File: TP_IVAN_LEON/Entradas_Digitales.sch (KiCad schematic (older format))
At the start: 7 parts, among them J1 Teclado

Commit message: Agregado codigo digey key en 80% de componentes
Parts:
- J1: Digikey# (none) -> WM1737-ND
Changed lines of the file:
@@
 F 2 "TP:Connector_Molex_PicoBlade_53047-0810" H 7750 3075 60  0001 C CNN
 F 3 "" H 7750 3075 60  0000 C CNN
+F 4 "WM1737-ND" H 7875 3075 60  0001 C CNN "Digikey#"
 	1    7875 3075
 	1    0    0    -1

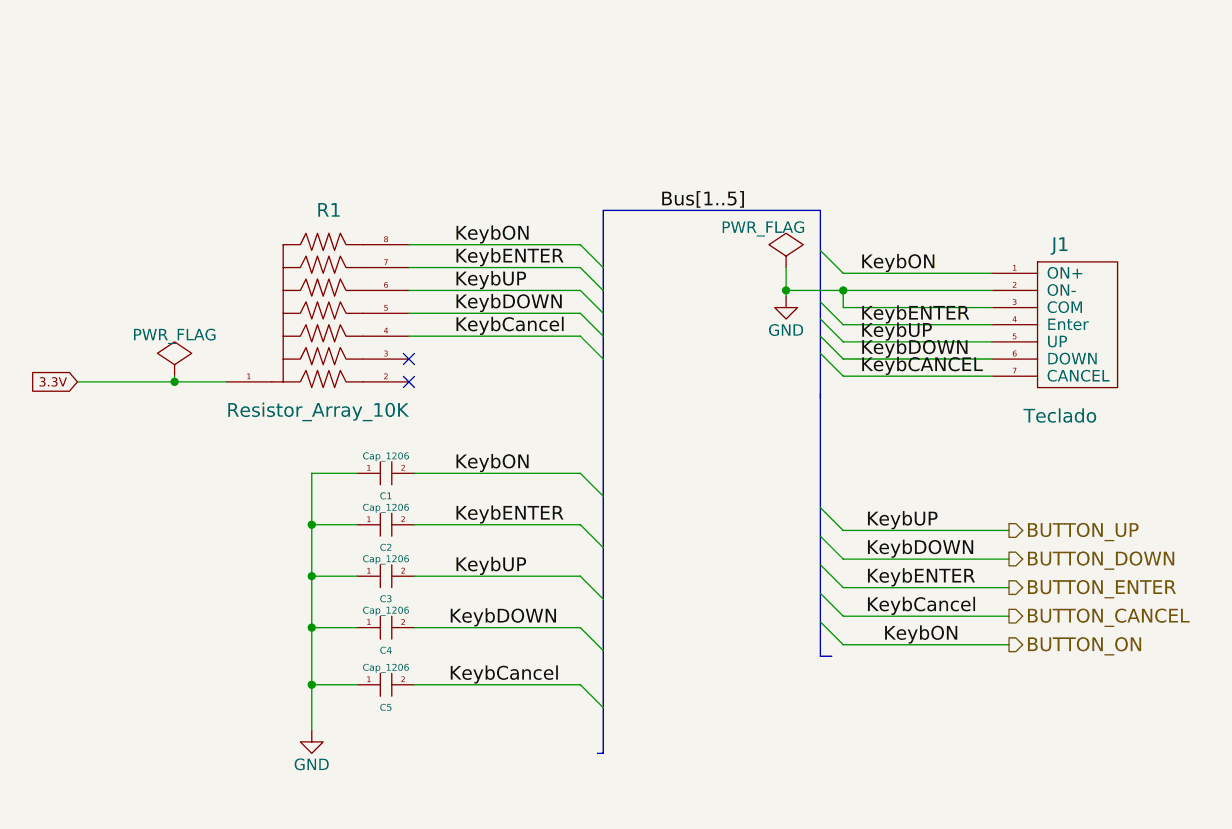
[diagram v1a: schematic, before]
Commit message: Agregado cambios subrayados en verde descritos en documento Leonv.ods en la carpeta docs
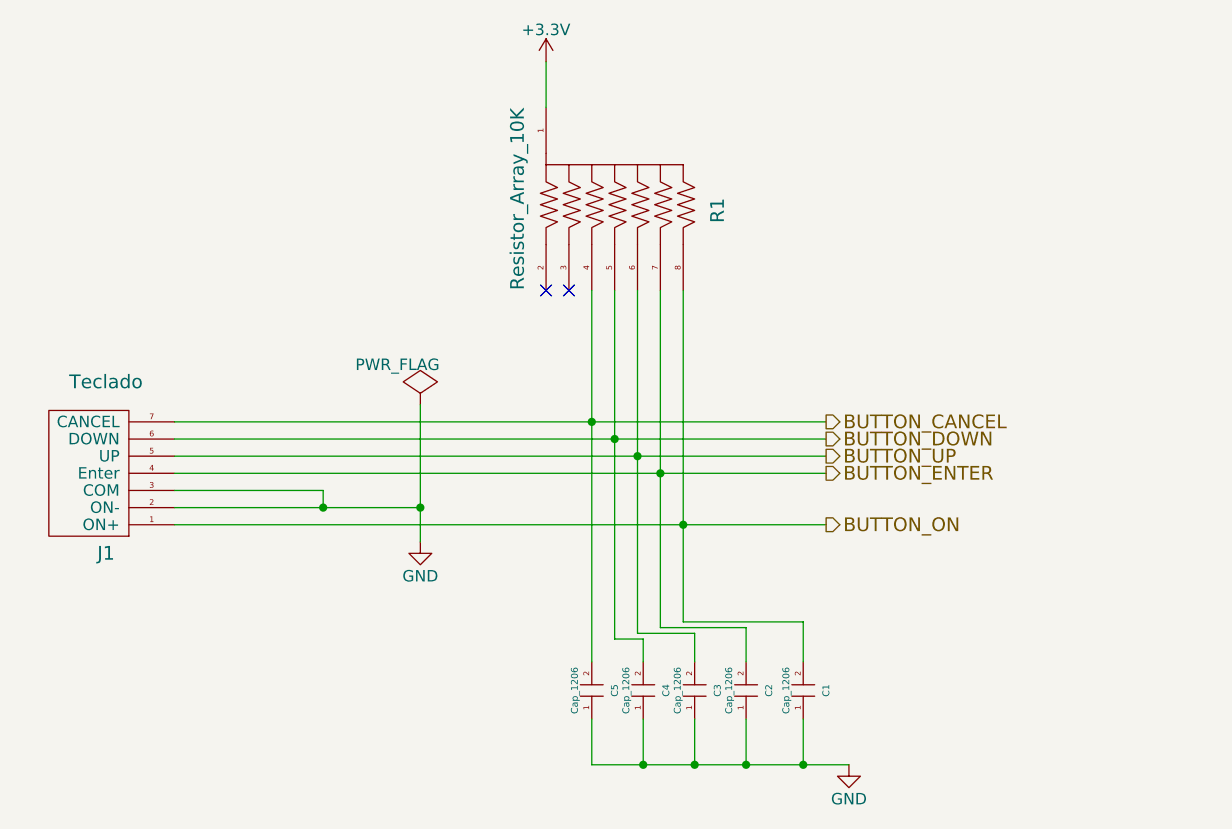
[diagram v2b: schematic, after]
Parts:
- renumbered C5 to C1, C4 to C2, C2 to C4, C1 to C5
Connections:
- net KeybCANCEL is gone; now on net BUTTON_CANCEL: J1.7 (CANCEL)
- net BUTTON_CANCEL: now also C5.2; no longer C1.2
- net BUTTON_DOWN: now also C4.2; no longer C2.2
- net BUTTON_ENTER: now also C2.2; no longer C4.2
- net BUTTON_ON: now also C1.2; no longer C5.2
- net 3.3V renamed +3V3
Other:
- moved on the sheet: C1, C2, C3, C4, C5, J1, R1

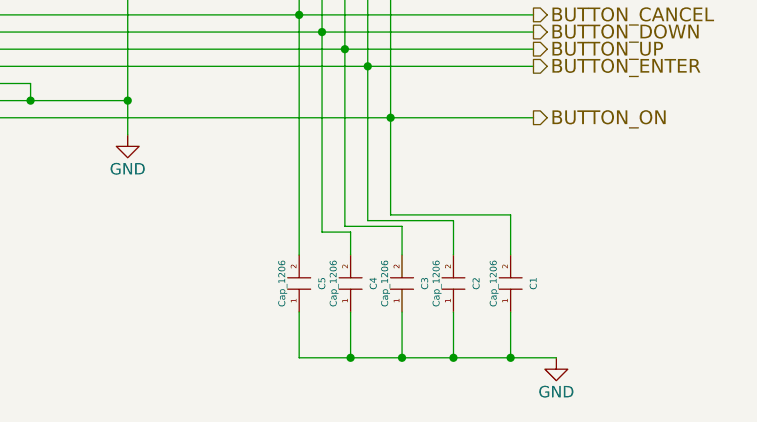
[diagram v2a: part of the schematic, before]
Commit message: Agrego Manf y Manf# en todos los componentes
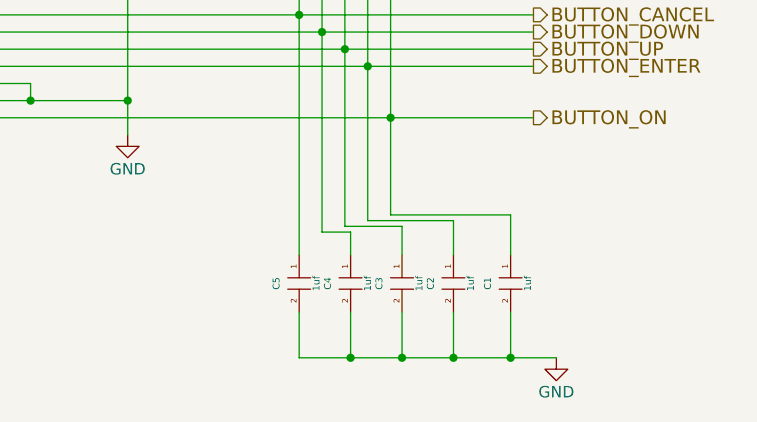
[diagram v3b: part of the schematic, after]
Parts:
- C1, C2, C3, C4, C5: value Cap_1206 -> 1uf; Digikey# (none) -> 399-1254-2-ND; Manf (none) -> Kemet; Manf# (none) -> C1206C105K4RACTU
- J1: Manf (none) -> Molex, LLC; Manf# (none) -> 0530470810
- R1: Digikey# (none) -> Y1747V0201BA0W-ND; Manf (none) -> Vishay Foil Resistors (Division of Vishay Precision Group); Manf# (none) -> Y1747V0201BA0W
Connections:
- net BUTTON_CANCEL: now also C5.1; no longer C5.2
- net BUTTON_DOWN: now also C4.1; no longer C4.2
- net BUTTON_ENTER: now also C2.1; no longer C2.2
- net BUTTON_ON: now also C1.1; no longer C1.2
- net BUTTON_UP: now also C3.1; no longer C3.2
- net GND: now also C1.2, C2.2, C3.2, C4.2, C5.2; no longer C1.1, C2.1, C3.1, C4.1, C5.1
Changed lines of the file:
@@
 F 3 "" H 3425 3675 60  0000 C CNN
 F 4 "WM1737-ND" H 3550 3675 60  0001 C CNN "Digikey#"
+F 5 "0530470810" H 3550 3675 60  0001 C CNN "Manf#"
+F 6 "Molex, LLC" H 3550 3675 60  0001 C CNN "Manf"
 	1    3550 3675
 	-1   0    0    1
@@
 F 2 "TP:Resistor_Array_SIP8" H 5900 2600 60  0001 C CNN
 F 3 "" H 5900 2600 60  0000 C CNN
+F 4 "Y1747V0201BA0W-ND" H 5975 2600 60  0001 C CNN "Digikey#"
+F 5 "Y1747V0201BA0W" H 5975 2600 60  0001 C CNN "Manf#"
+F 6 "Vishay Foil Resistors (Division of Vishay Precision Group)" H 5975 2600 60  0001 C CNN "Manf"
 	1    5975 2600
 	0    1    1    0
-$EndComp
-$Comp
-L Cap_1206 C5
-U 1 1 57846246
-P 5750 4650
-F 0 "C5" H 5750 4550 30  0000 C CNN
-F 1 "Cap_1206" H 5750 4725 30  0000 C CNN
-F 2 "TP:c_1206" H 5775 4650 60  0001 C CNN
-F 3 "" H 5775 4650 60  0000 C CNN
-	1    5750 4650
-	0    -1   -1   0
-$EndComp
-$Comp
-L Cap_1206 C4
-U 1 1 578462E7
-P 5975 4650
-F 0 "C4" H 5975 4550 30  0000 C CNN
-F 1 "Cap_1206" H 5975 4725 30  0000 C CNN
-F 2 "TP:c_1206" H 6000 4650 60  0001 C CNN
-F 3 "" H 6000 4650 60  0000 C CNN
-	1    5975 4650
-	0    -1   -1   0
-$EndComp
-$Comp
-L Cap_1206 C3
-U 1 1 5784638A
-P 6200 4650
-F 0 "C3" H 6200 4550 30  0000 C CNN
-F 1 "Cap_1206" H 6200 4725 30  0000 C CNN
-F 2 "TP:c_1206" H 6225 4650 60  0001 C CNN
-F 3 "" H 6225 4650 60  0000 C CNN
-	1    6200 4650
-	0    -1   -1   0
-$EndComp
-$Comp
-L Cap_1206 C2
-U 1 1 578463B7
-P 6425 4650
-F 0 "C2" H 6425 4550 30  0000 C CNN
-F 1 "Cap_1206" H 6425 4725 30  0000 C CNN
-F 2 "TP:c_1206" H 6450 4650 60  0001 C CNN
-F 3 "" H 6450 4650 60  0000 C CNN
-	1    6425 4650
-	0    -1   -1   0
 $EndComp
 $Comp
@@
 $EndComp
 $Comp
-L Cap_1206 C1
-U 1 1 57846C45
-P 6675 4650
-F 0 "C1" H 6675 4550 30  0000 C CNN
-F 1 "Cap_1206" H 6675 4725 30  0000 C CNN
-F 2 "TP:c_1206" H 6700 4650 60  0001 C CNN
-F 3 "" H 6700 4650 60  0000 C CNN
-	1    6675 4650
-	0    -1   -1   0
-$EndComp
-$Comp
 L GND #PWR02
 U 1 1 57858E16
@@
 	5750 2900 5750 4525
 Connection ~ 5750 3475
+$Comp
+L Cap_1206 C1
+U 1 1 57BFD912
+P 6675 4650
+F 0 "C1" H 6675 4550 30  0000 C CNN
+F 1 "1uf" H 6675 4725 30  0000 C CNN
+F 2 "TP:c_1206" H 6700 4650 60  0001 C CNN
+F 3 "" H 6700 4650 60  0000 C CNN
+F 4 "399-1254-2-ND" H 6675 4650 60  0001 C CNN "Digikey#"
+F 5 "C1206C105K4RACTU" H 6675 4650 60  0001 C CNN "Manf#"
+F 6 "Kemet" H 6675 4650 60  0001 C CNN "Manf"
+	1    6675 4650
+	0    1    1    0
+$EndComp
+$Comp
+L Cap_1206 C2
+U 1 1 57BFDB70
+P 6425 4650
+F 0 "C2" H 6425 4550 30  0000 C CNN
+F 1 "1uf" H 6425 4725 30  0000 C CNN
+F 2 "TP:c_1206" H 6450 4650 60  0001 C CNN
+F 3 "" H 6450 4650 60  0000 C CNN
+F 4 "399-1254-2-ND" H 6425 4650 60  0001 C CNN "Digikey#"
+F 5 "C1206C105K4RACTU" H 6425 4650 60  0001 C CNN "Manf#"
+F 6 "Kemet" H 6425 4650 60  0001 C CNN "Manf"
+	1    6425 4650
+	0    1    1    0
+$EndComp
+$Comp
+L Cap_1206 C3
+U 1 1 57BFDB9A
+P 6200 4650
+F 0 "C3" H 6200 4550 30  0000 C CNN
+F 1 "1uf" H 6200 4725 30  0000 C CNN
+F 2 "TP:c_1206" H 6225 4650 60  0001 C CNN
+F 3 "" H 6225 4650 60  0000 C CNN
+F 4 "399-1254-2-ND" H 6200 4650 60  0001 C CNN "Digikey#"
+F 5 "C1206C105K4RACTU" H 6200 4650 60  0001 C CNN "Manf#"
+F 6 "Kemet" H 6200 4650 60  0001 C CNN "Manf"
+	1    6200 4650
+	0    1    1    0
+$EndComp
+$Comp
+L Cap_1206 C4
+U 1 1 57BFDBCB
+P 5975 4650
+F 0 "C4" H 5975 4550 30  0000 C CNN
+F 1 "1uf" H 5975 4725 30  0000 C CNN
+F 2 "TP:c_1206" H 6000 4650 60  0001 C CNN
+F 3 "" H 6000 4650 60  0000 C CNN
+F 4 "399-1254-2-ND" H 5975 4650 60  0001 C CNN "Digikey#"
+F 5 "C1206C105K4RACTU" H 5975 4650 60  0001 C CNN "Manf#"
+F 6 "Kemet" H 5975 4650 60  0001 C CNN "Manf"
+	1    5975 4650
+	0    1    1    0
+$EndComp
+$Comp
+L Cap_1206 C5
+U 1 1 57BFDBFB
+P 5750 4650
+F 0 "C5" H 5750 4550 30  0000 C CNN
+F 1 "1uf" H 5750 4725 30  0000 C CNN
+F 2 "TP:c_1206" H 5775 4650 60  0001 C CNN
+F 3 "" H 5775 4650 60  0000 C CNN
+F 4 "399-1254-2-ND" H 5750 4650 60  0001 C CNN "Digikey#"
+F 5 "C1206C105K4RACTU" H 5750 4650 60  0001 C CNN "Manf#"
+F 6 "Kemet" H 5750 4650 60  0001 C CNN "Manf"
+	1    5750 4650
+	0    1    1    0
+$EndComp
 $EndSCHEMATC
